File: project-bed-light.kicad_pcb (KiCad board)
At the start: 2 copper layers, 58 x 56 mm, 24 parts, among them J1 2060-452_998-404, J2 WAGO_2060-453-998-404, J3 Conn_01x03_Pin, Q1 Q_Toshiba_SSM3J328R, U1 TPS62933, U2 Pink Panda v2.1.0

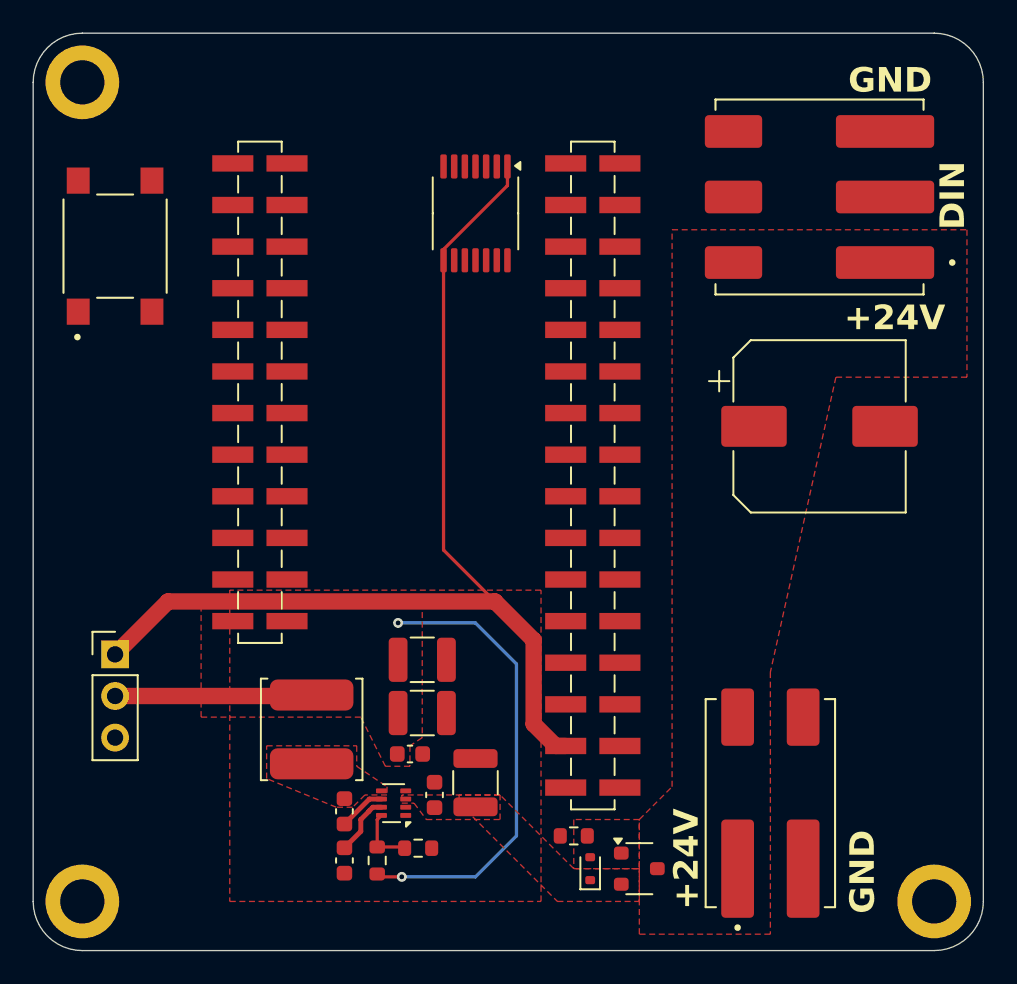
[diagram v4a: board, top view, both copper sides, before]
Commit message: pcb: finish routing
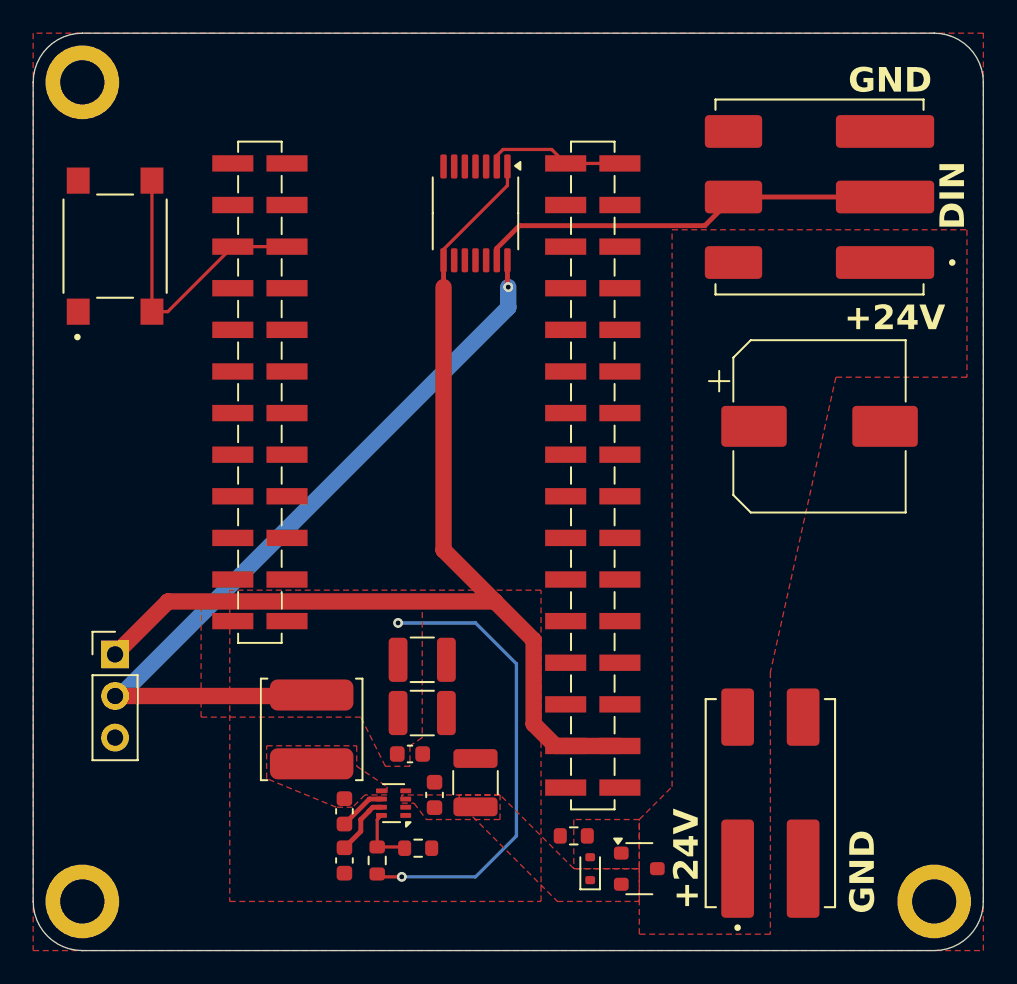
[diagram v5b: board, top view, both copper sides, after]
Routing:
- net +5V: track 40.4 -> 77.1 mm, vias 2 -> 3
- net /D_{IN}: track 0.00 -> 25.7 mm
- net Net-(U2-P0.04): track 0.00 -> 17.9 mm
- net Net-(U2-P0.20): track 0.00 -> 8.68 mm
- net +3.3V: track 65.0 -> 69.9 mm
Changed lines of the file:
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@@
 			(pinfunction "SW")
 			(pintype "output")
+			(zone_connect 2)
 			(thermal_bridge_angle 45)
 		)
@@
 	)
 	(segment
+		(start 49.95 36.45)
+		(end 50 36.5)
+		(width 0.3)
+		(layer "F.Cu")
+		(net 6)
+	)
+	(segment
 		(start 42.175 72.5)
 		(end 43.5 72.5)
 		(width 0.2)
+		(layer "F.Cu")
+		(net 6)
+	)
+	(segment
+		(start 49.95 34.8625)
+		(end 49.95 36.45)
+		(width 0.3)
 		(layer "F.Cu")
 		(net 6)
@@
 		(net 6)
 	)
+	(via
+		(at 50 36.5)
+		(size 0.6)
+		(drill 0.3)
+		(layers "F.Cu" "B.Cu")
+		(net 6)
+	)
+	(segment
+		(start 50 37.75)
+		(end 50 36.5)
+		(width 1)
+		(layer "B.Cu")
+		(net 6)
+	)
 	(segment
 		(start 50.5 70)
@@
 	)
 	(segment
+		(start 26 61.46)
+		(end 26.29 61.46)
+		(width 1)
+		(layer "B.Cu")
+		(net 6)
+	)
+	(segment
 		(start 48 57)
 		(end 50.5 59.5)
@@
 	)
 	(segment
+		(start 26.29 61.46)
+		(end 50 37.75)
+		(width 1)
+		(layer "B.Cu")
+		(net 6)
+	)
+	(segment
 		(start 50.5 59.5)
 		(end 50.5 70)
@@
 	)
 	(segment
+		(start 63.75 31)
+		(end 73 31)
+		(width 0.3)
+		(layer "F.Cu")
+		(net 9)
+	)
+	(segment
+		(start 63.75 31)
+		(end 62 32.75)
+		(width 0.3)
+		(layer "F.Cu")
+		(net 9)
+	)
+	(segment
+		(start 49.3 34.134418)
+		(end 49.3 34.8625)
+		(width 0.3)
+		(layer "F.Cu")
+		(net 9)
+	)
+	(segment
+		(start 50.684418 32.75)
+		(end 49.3 34.134418)
+		(width 0.3)
+		(layer "F.Cu")
+		(net 9)
+	)
+	(segment
+		(start 62 32.75)
+		(end 50.684418 32.75)
+		(width 0.3)
+		(layer "F.Cu")
+		(net 9)
+	)
+	(segment
+		(start 26 58.92)
+		(end 29.231 55.689)
+		(width 1)
+		(layer "F.Cu")
+		(net 10)
+	)
+	(segment
+		(start 46.05 34.8625)
+		(end 46.05 34.2)
+		(width 0.2)
+		(layer "F.Cu")
+		(net 10)
+	)
+	(segment
+		(start 52.888 64.51)
+		(end 53.505 64.51)
+		(width 1)
+		(layer "F.Cu")
+		(net 10)
+	)
+	(segment
+		(start 51.549 58.049)
+		(end 51.549 63.171)
+		(width 1)
+		(layer "F.Cu")
+		(net 10)
+	)
+	(segment
+		(start 49.189 55.689)
+		(end 51.549 58.049)
+		(width 1)
+		(layer "F.Cu")
+		(net 10)
+	)
+	(segment
+		(start 29.231 55.689)
+		(end 49.189 55.689)
+		(width 1)
+		(layer "F.Cu")
+		(net 10)
+	)
+	(segment
 		(start 46.05 52.55)
 		(end 49.189 55.689)
-		(width 0.2)
-		(layer "F.Cu")
-		(net 10)
-	)
-	(segment
-		(start 26 58.92)
-		(end 29.231 55.689)
-		(width 1)
-		(layer "F.Cu")
-		(net 10)
-	)
-	(segment
-		(start 46.05 34.8625)
-		(end 46.05 34.2)
-		(width 0.2)
-		(layer "F.Cu")
-		(net 10)
-	)
-	(segment
-		(start 52.888 64.51)
-		(end 53.505 64.51)
-		(width 1)
-		(layer "F.Cu")
-		(net 10)
-	)
-	(segment
-		(start 51.549 58.049)
-		(end 51.549 63.171)
-		(width 1)
-		(layer "F.Cu")
-		(net 10)
-	)
-	(segment
-		(start 49.189 55.689)
-		(end 51.549 58.049)
-		(width 1)
-		(layer "F.Cu")
-		(net 10)
-	)
-	(segment
-		(start 29.231 55.689)
-		(end 49.189 55.689)
-		(width 1)
-		(layer "F.Cu")
-		(net 10)
-	)
-	(segment
-		(start 46.05 34.8625)
-		(end 46.05 52.55)
-		(width 0.2)
+		(width 1)
 		(layer "F.Cu")
 		(net 10)
@@
 	)
 	(segment
+		(start 46.05 36.5)
+		(end 46.05 52.55)
+		(width 1)
+		(layer "F.Cu")
+		(net 10)
+	)
+	(segment
+		(start 46.05 37.3)
+		(end 46.05 36.5)
+		(width 0.2)
+		(layer "F.Cu")
+		(net 10)
+	)
+	(segment
 		(start 49.95 30.3)
 		(end 49.95 29.1375)
@@
 	)
 	(segment
+		(start 53.505 64.51)
+		(end 56.815 64.51)
+		(width 1)
+		(layer "F.Cu")
+		(net 10)
+	)
+	(segment
 		(start 51.549 63.171)
 		(end 52.888 64.51)
@@
 	)
 	(segment
+		(start 46.05 34.8625)
+		(end 46.05 37.3)
+		(width 0.3)
+		(layer "F.Cu")
+		(net 10)
+	)
+	(segment
 		(start 42 70.675)
 		(end 43.6 70.675)
@@
 		(layer "F.Cu")
 		(net 11)
+	)
+	(segment
+		(start 28.25 30)
+		(end 28.25 38)
+		(width 0.2)
+		(layer "F.Cu")
+		(net 12)
+	)
+	(segment
+		(start 28.25 38)
+		(end 29.215 38)
+		(width 0.2)
+		(layer "F.Cu")
+		(net 12)
+	)
+	(segment
+		(start 33.185 34.03)
+		(end 36.495 34.03)
+		(width 0.2)
+		(layer "F.Cu")
+		(net 12)
+	)
+	(segment
+		(start 29.215 38)
+		(end 33.185 34.03)
+		(width 0.2)
+		(layer "F.Cu")
+		(net 12)
+	)
+	(segment
+		(start 49.68113 28.099)
+		(end 52.654 28.099)
+		(width 0.2)
+		(layer "F.Cu")
+		(net 33)
+	)
+	(segment
+		(start 49.3 29.1375)
+		(end 49.3 28.48013)
+		(width 0.2)
+		(layer "F.Cu")
+		(net 33)
+	)
+	(segment
+		(start 52.654 28.099)
+		(end 53.505 28.95)
+		(width 0.2)
+		(layer "F.Cu")
+		(net 33)
+	)
+	(segment
+		(start 53.505 28.95)
+		(end 56.815 28.95)
+		(width 0.2)
+		(layer "F.Cu")
+		(net 33)
+	)
+	(segment
+		(start 49.3 28.48013)
+		(end 49.68113 28.099)
+		(width 0.2)
+		(layer "F.Cu")
+		(net 33)
 	)
 	(zone
@@
 			)
 		)
+	)
+	(zone
+		(net 1)
+		(net_name "GND")
+		(layer "F.Cu")
+		(hatch edge 0.5)
+		(connect_pads
+			(clearance 0.2)
+		)
+		(min_thickness 0.2)
+		(filled_areas_thickness no)
+		(fill yes
+			(thermal_gap 0.2)
+			(thermal_bridge_width 0.2)
+			(smoothing fillet)
+			(radius 0.5)
+		)
+		(polygon
+			(pts
+				(xy 79 77) (xy 79 21) (xy 21 21) (xy 21 77)
+			)
+		)

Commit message: pcb: add all GND vias
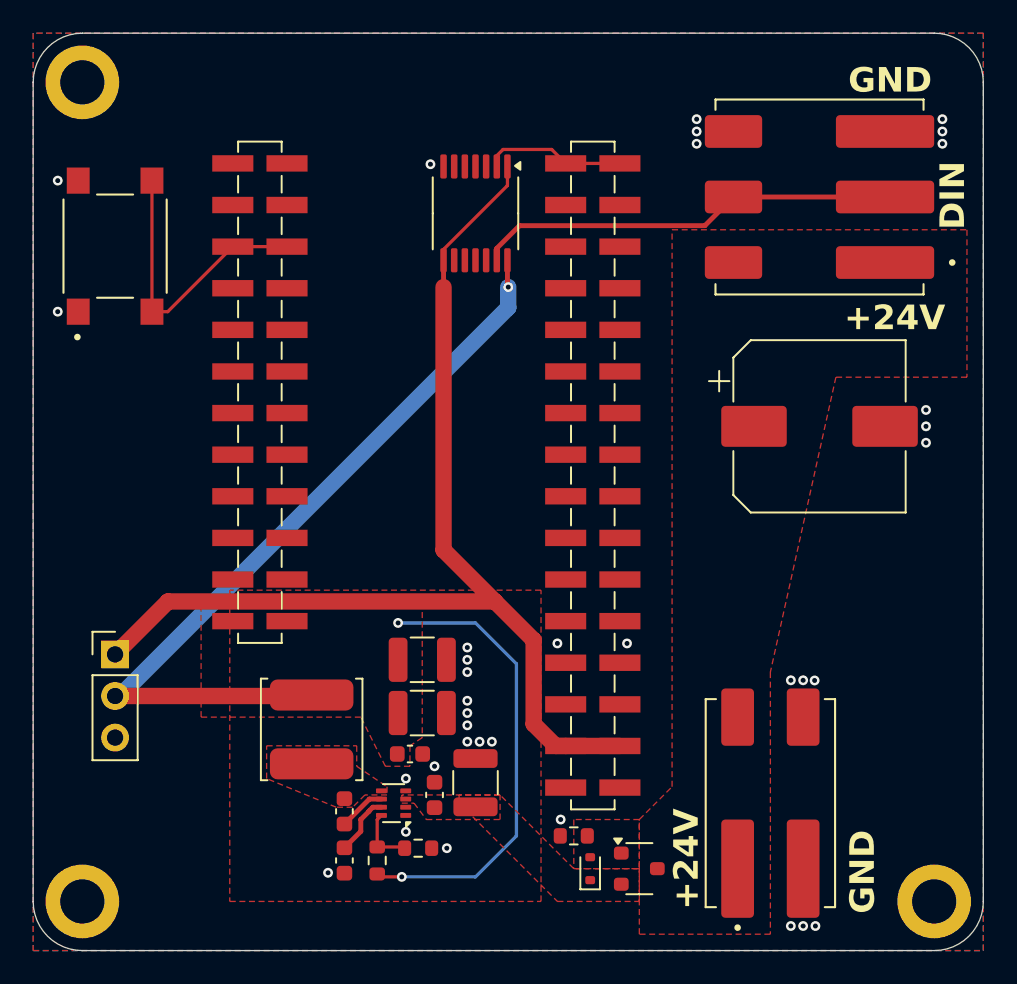
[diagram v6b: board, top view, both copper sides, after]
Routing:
- net GND: vias 0 -> 35
- added copper zone on B.Cu, net GND
